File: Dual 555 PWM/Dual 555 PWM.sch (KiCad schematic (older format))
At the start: 13 parts, among them J1 Conn_01x04_Male, U1 TLC555, U2 TLC555

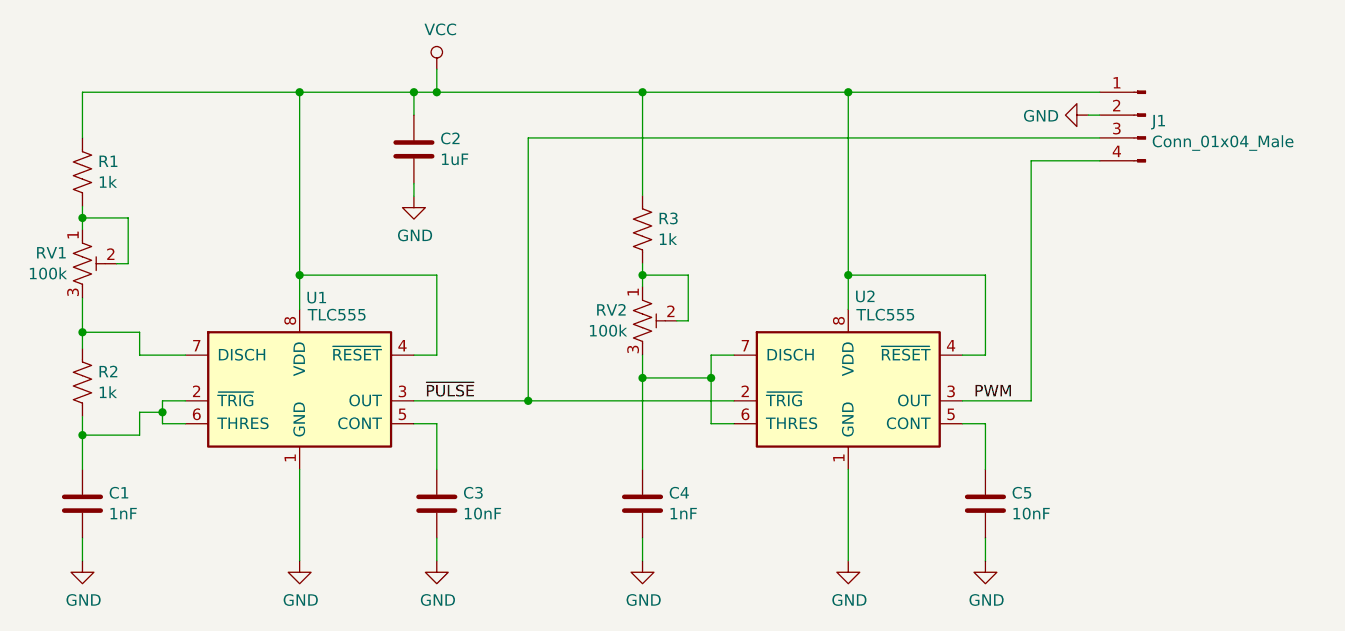
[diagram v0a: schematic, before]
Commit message: Silk screen edits
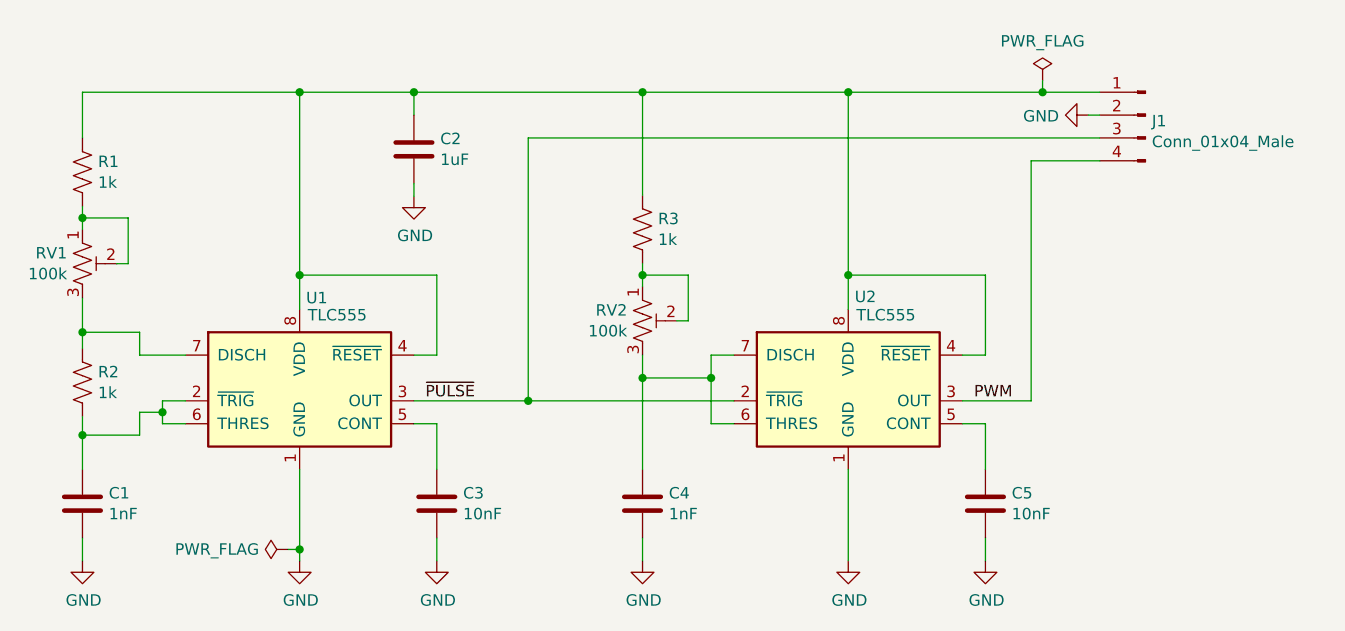
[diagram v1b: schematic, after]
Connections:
- net VCC: no longer names the net of C2.1, J1.1 (Pin_1), R1.1, R3.1, U1.4 (~RESET), U1.8 (VDD), U2.4 (~RESET), U2.8 (VDD)
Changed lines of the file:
@@
 Wire Wire Line
 	4600 3300 4600 3500
-$Comp
-L power:VCC #PWR04
-U 1 1 6035C72D
-P 4600 1750
-F 0 "#PWR04" H 4600 1600 50  0001 C CNN
-F 1 "VCC" H 4617 1923 50  0000 C CNN
-F 2 "" H 4600 1750 50  0001 C CNN
-F 3 "" H 4600 1750 50  0001 C CNN
-	1    4600 1750
-	1    0    0    -1
-$EndComp
 Wire Wire Line
 	4500 3000 4600 3000
@@
 	1    0    0    -1
 $EndComp
-Wire Wire Line
-	4000 3900 4000 3500
 $Comp
 L power:GND #PWR05
@@
 	5500 2300 5500 1850
 Wire Wire Line
-	4000 1850 4500 1850
-Wire Wire Line
-	5500 1850 6400 1850
-Wire Wire Line
 	6400 1850 6400 2650
-Wire Wire Line
-	4600 1750 4600 1850
 $Comp
 L Device:C C2
@@
 	4500 1950 4500 1850
 Connection ~ 4500 1850
-Wire Wire Line
-	4500 1850 4600 1850
 $Comp
 L power:GND #PWR03
@@
 $EndComp
 Wire Wire Line
-	7500 1850 6400 1850
+	7500 1850 7250 1850
 Connection ~ 6400 1850
 $Comp
@@
 Wire Wire Line
 	5000 2050 5000 3200
-Wire Wire Line
-	4600 1850 5500 1850
-Connection ~ 4600 1850
 Connection ~ 5500 1850
 Wire Wire Line
@@
 Wire Wire Line
 	3050 2750 3050 2900
+$Comp
+L power:PWR_FLAG #FLG0101
+U 1 1 604984CF
+P 7250 1800
+F 0 "#FLG0101" H 7250 1875 50  0001 C CNN
+F 1 "PWR_FLAG" H 7250 1973 50  0000 C CNN
+F 2 "" H 7250 1800 50  0001 C CNN
+F 3 "~" H 7250 1800 50  0001 C CNN
+	1    7250 1800
+	1    0    0    -1
+$EndComp
+Wire Wire Line
+	4000 1850 4500 1850
+Wire Wire Line
+	4500 1850 5500 1850
+Wire Wire Line
+	5500 1850 6400 1850
+Wire Wire Line
+	7250 1800 7250 1850
+Connection ~ 7250 1850
+Wire Wire Line
+	7250 1850 6400 1850
+$Comp
+L power:PWR_FLAG #FLG0102
+U 1 1 604A02A6
+P 3950 3850
+F 0 "#FLG0102" H 3950 3925 50  0001 C CNN
+F 1 "PWR_FLAG" V 3950 3977 50  0000 L CNN
+F 2 "" H 3950 3850 50  0001 C CNN
+F 3 "~" H 3950 3850 50  0001 C CNN
+	1    3950 3850
+	0    -1   -1   0
+$EndComp
+Wire Wire Line
+	3950 3850 4000 3850
+Wire Wire Line
+	4000 3500 4000 3850
+Connection ~ 4000 3850
+Wire Wire Line
+	4000 3850 4000 3900
 $EndSCHEMATC
